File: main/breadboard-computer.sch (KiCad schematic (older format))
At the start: 0 parts

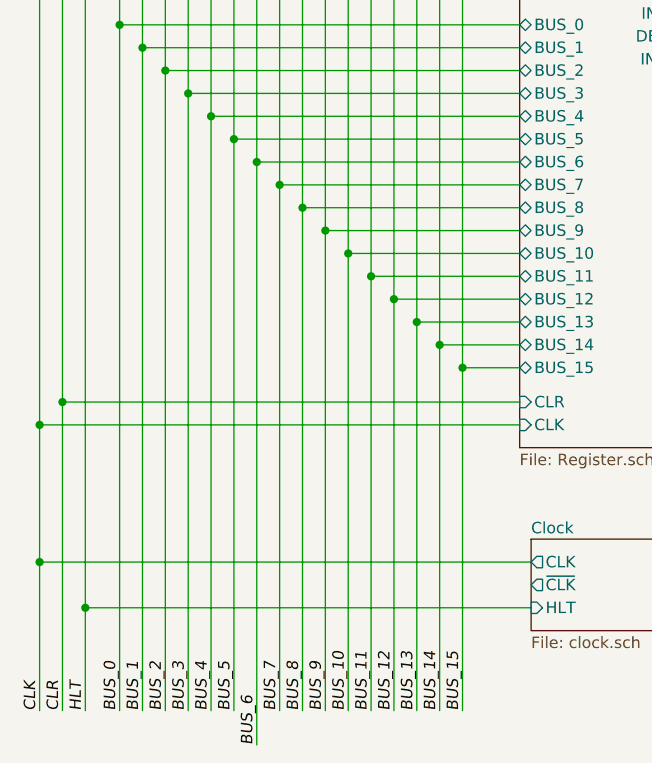
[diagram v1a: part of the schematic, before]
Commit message: Switch to using 74LS377 in place of two 74LS173
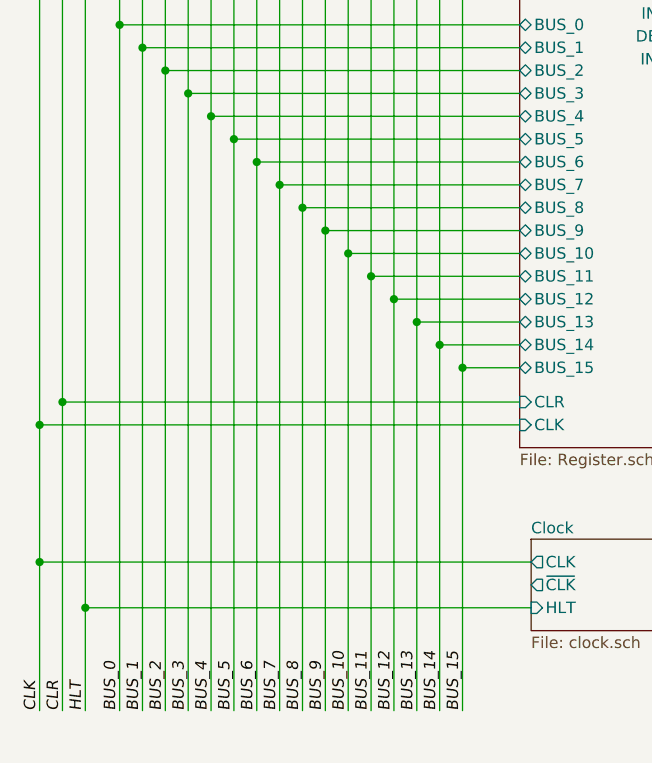
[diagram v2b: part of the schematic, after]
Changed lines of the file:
@@
 EESchema Schematic File Version 4
-LIBS:breadboard-computer-cache
 EELAYER 30 0
 EELAYER END
@@
 Sheet 1 26
 Title "High Level Overview"
-Date "2019-11-17"
-Rev "v1.0"
+Date "2020-02-23"
+Rev "v1.1"
 Comp "Christopher Milan"
 Comment1 "Computer Science 4"
@@
 Text Label 1500 10400 1    50   Italic 0
 BUS_5
-Text Label 1600 10550 1    50   Italic 0
+Text Label 1600 10400 1    50   Italic 0
 BUS_6
 Text Label 1700 10400 1    50   Italic 0
@@
 	1500 10400 1500 7900
 Wire Wire Line
-	1600 8000 1600 10550
+	1600 8000 1600 10400
 Wire Wire Line
 	1700 10400 1700 8100
